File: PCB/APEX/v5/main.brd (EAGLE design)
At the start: 160 x 100 mm, 4 parts

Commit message: completed pcb
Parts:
- moved CN1 140.9 mm to (63.5, 124.5), flipped to the bottom
- moved JP6 51.8 mm to (69.7, 116.8), turned to 180 degrees
- moved JP2 48.9 mm to (55.1, 109.2), flipped to the bottom, turned to 270 degrees
- moved JP5 44.2 mm to (69.7, 101.6), turned to 0 degrees
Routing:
- net AIN+: track 0.00 -> 10.1 mm
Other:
- board size 160 x 100 mm -> 38.1 x 38.1 mm

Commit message: pours
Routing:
- added copper zone on layer 16, net GND
- added copper zone on layer 1, net VCC
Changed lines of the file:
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@@
 <signals>
 <signal name="VCC">
-<wire x1="62.0395" y1="118.11" x2="55.118" y2="111.76" width="0" layer="19" extent="1-1"/>
-<wire x1="62.0395" y1="118.11" x2="62.0395" y2="116.84" width="0" layer="19" extent="1-1"/>
-<wire x1="62.5" y1="124.46" x2="62.0395" y2="116.84" width="0" layer="19" extent="1-1"/>
 <contactref element="JP2" pad="2"/>
 <contactref element="JP6" pad="7"/>
 <contactref element="JP6" pad="7C"/>
 <contactref element="CN1" pad="1"/>
+<polygon width="1.27" layer="1" isolate="1.016">
+<vertex x="40.64" y="133.35"/>
+<vertex x="40.64" y="90.17"/>
+<vertex x="92.71" y="90.17"/>
+<vertex x="92.71" y="132.08"/>
+<vertex x="91.44" y="133.35"/>
+</polygon>
 </signal>
 <signal name="GND">
@@
 <contactref element="CN1" pad="2"/>
 <contactref element="JP2" pad="4"/>
-<wire x1="55.118" y1="114.3" x2="55.118" y2="106.68" width="0" layer="19" extent="1-1"/>
-<wire x1="64.5795" y1="118.11" x2="55.118" y2="106.68" width="0" layer="19" extent="1-1"/>
-<wire x1="64.5795" y1="118.11" x2="64.5795" y2="116.84" width="0" layer="19" extent="1-1"/>
-<wire x1="64.5" y1="124.46" x2="64.5795" y2="116.84" width="0" layer="19" extent="1-1"/>
+<polygon width="1.27" layer="16" isolate="1.016">
+<vertex x="41.91" y="132.08"/>
+<vertex x="41.91" y="90.17"/>
+<vertex x="43.18" y="88.9"/>
+<vertex x="90.17" y="88.9"/>
+<vertex x="92.71" y="91.44"/>
+<vertex x="92.71" y="132.08"/>
+</polygon>
 </signal>
 <signal name="SD">
@@
 </signal>
 <signal name="MOSI">
-<wire x1="69.6595" y1="118.11" x2="69.6595" y2="116.84" width="0" layer="19" extent="1-1"/>
 <contactref element="JP6" pad="4"/>
 <contactref element="JP6" pad="4C"/>
+<wire x1="69.6595" y1="118.11" x2="69.6595" y2="116.84" width="0" layer="19" extent="1-1"/>
 </signal>
 <signal name="MISO">
-<wire x1="72.1995" y1="118.11" x2="72.1995" y2="116.84" width="0" layer="19" extent="1-1"/>
 <contactref element="JP6" pad="3"/>
 <contactref element="JP6" pad="3C"/>
+<wire x1="72.1995" y1="118.11" x2="72.1995" y2="116.84" width="0" layer="19" extent="1-1"/>
 </signal>
 <signal name="SCK">
-<wire x1="74.7395" y1="118.11" x2="74.7395" y2="116.84" width="0" layer="19" extent="1-1"/>
 <contactref element="JP6" pad="2"/>
 <contactref element="JP6" pad="2C"/>
+<wire x1="74.7395" y1="118.11" x2="74.7395" y2="116.84" width="0" layer="19" extent="1-1"/>
 </signal>
 <signal name="A2">
@@
 <contactref element="JP5" pad="6"/>
 <contactref element="JP5" pad="6C"/>
-<wire x1="74.7395" y1="101.6" x2="74.7395" y2="100.33" width="0" layer="19" extent="1-1"/>
+<wire x1="74.7395" y1="100.33" x2="74.7395" y2="101.6" width="0" layer="19" extent="1-1"/>
 </signal>
 <signal name="+3V3">
-<wire x1="67.1195" y1="118.11" x2="67.1195" y2="116.84" width="0" layer="19" extent="1-1"/>
 <contactref element="JP6" pad="5"/>
 <contactref element="JP6" pad="5C"/>
+<wire x1="67.1195" y1="118.11" x2="67.1195" y2="116.84" width="0" layer="19" extent="1-1"/>
 </signal>
 <signal name="PB22/I6/SERCOM5.1">
@@
 <contactref element="JP5" pad="7"/>
 <contactref element="JP5" pad="7C"/>
-<wire x1="77.2795" y1="101.6" x2="77.2795" y2="100.33" width="0" layer="19" extent="1-1"/>
+<wire x1="77.2795" y1="100.33" x2="77.2795" y2="101.6" width="0" layer="19" extent="1-1"/>
 </signal>
 <signal name="RX">
-<wire x1="77.2795" y1="118.11" x2="77.2795" y2="116.84" width="0" layer="19" extent="1-1"/>
 <contactref element="JP6" pad="1"/>
 <contactref element="JP6" pad="1C"/>
+<wire x1="77.2795" y1="118.11" x2="77.2795" y2="116.84" width="0" layer="19" extent="1-1"/>
 </signal>
 </signals>

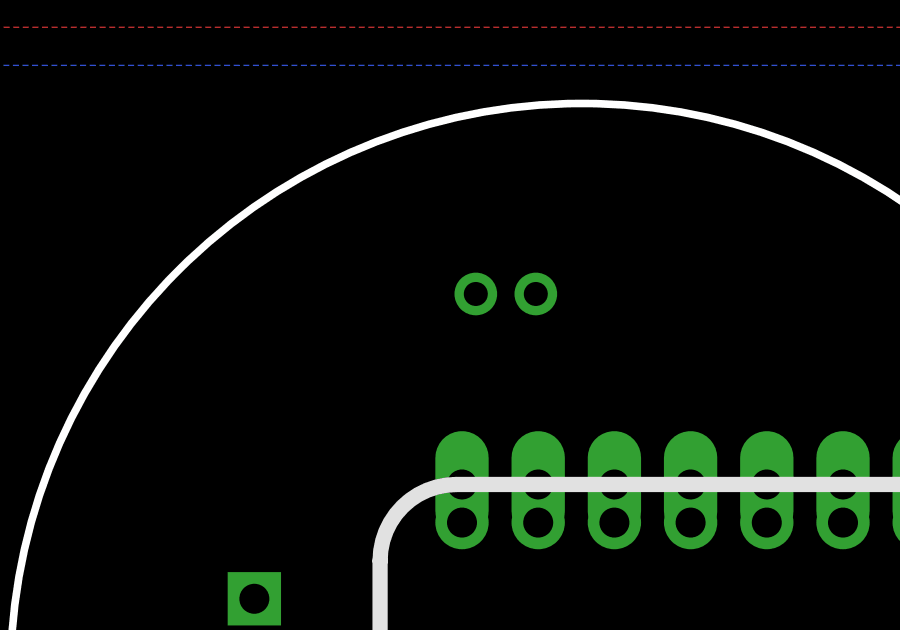
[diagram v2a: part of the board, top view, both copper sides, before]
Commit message: flip battery connector
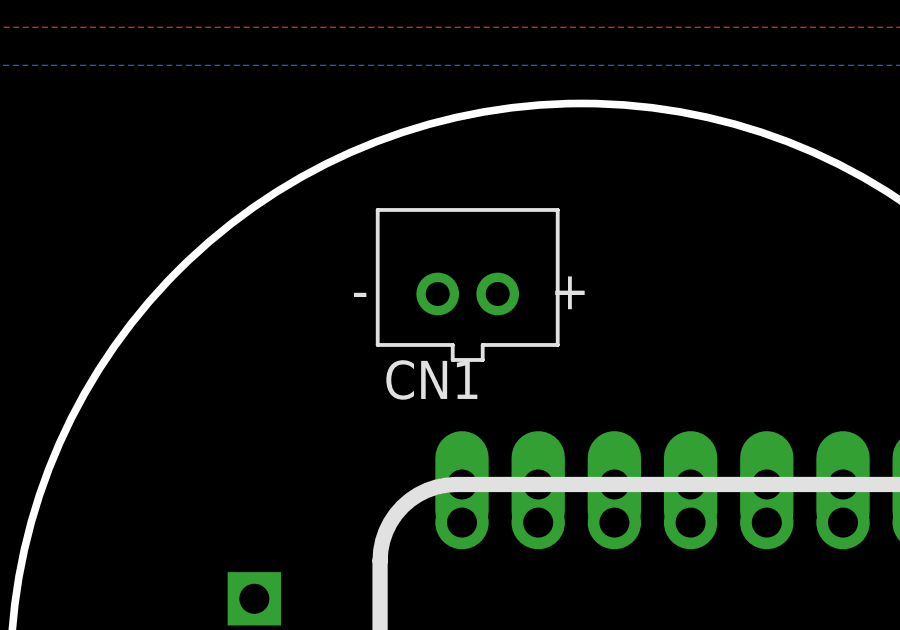
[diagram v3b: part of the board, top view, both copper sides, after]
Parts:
- moved CN1 1.27 mm to (62.2, 124.5), flipped to the top
